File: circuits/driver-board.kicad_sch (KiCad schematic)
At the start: 73 parts, among them J1 Conn_01x18_Female, J2 USB4120-03-C_REVA, J3 Motor_Conn_01x04, J4 Screw_Terminals, J5 Conn_01x06_Female, Q1 SS8050-G, Q2 SS8050-G, SW1 RST_SW_Push, U1 CP2102N-Axx-xQFN24, U2 BA033CC0FP-E2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

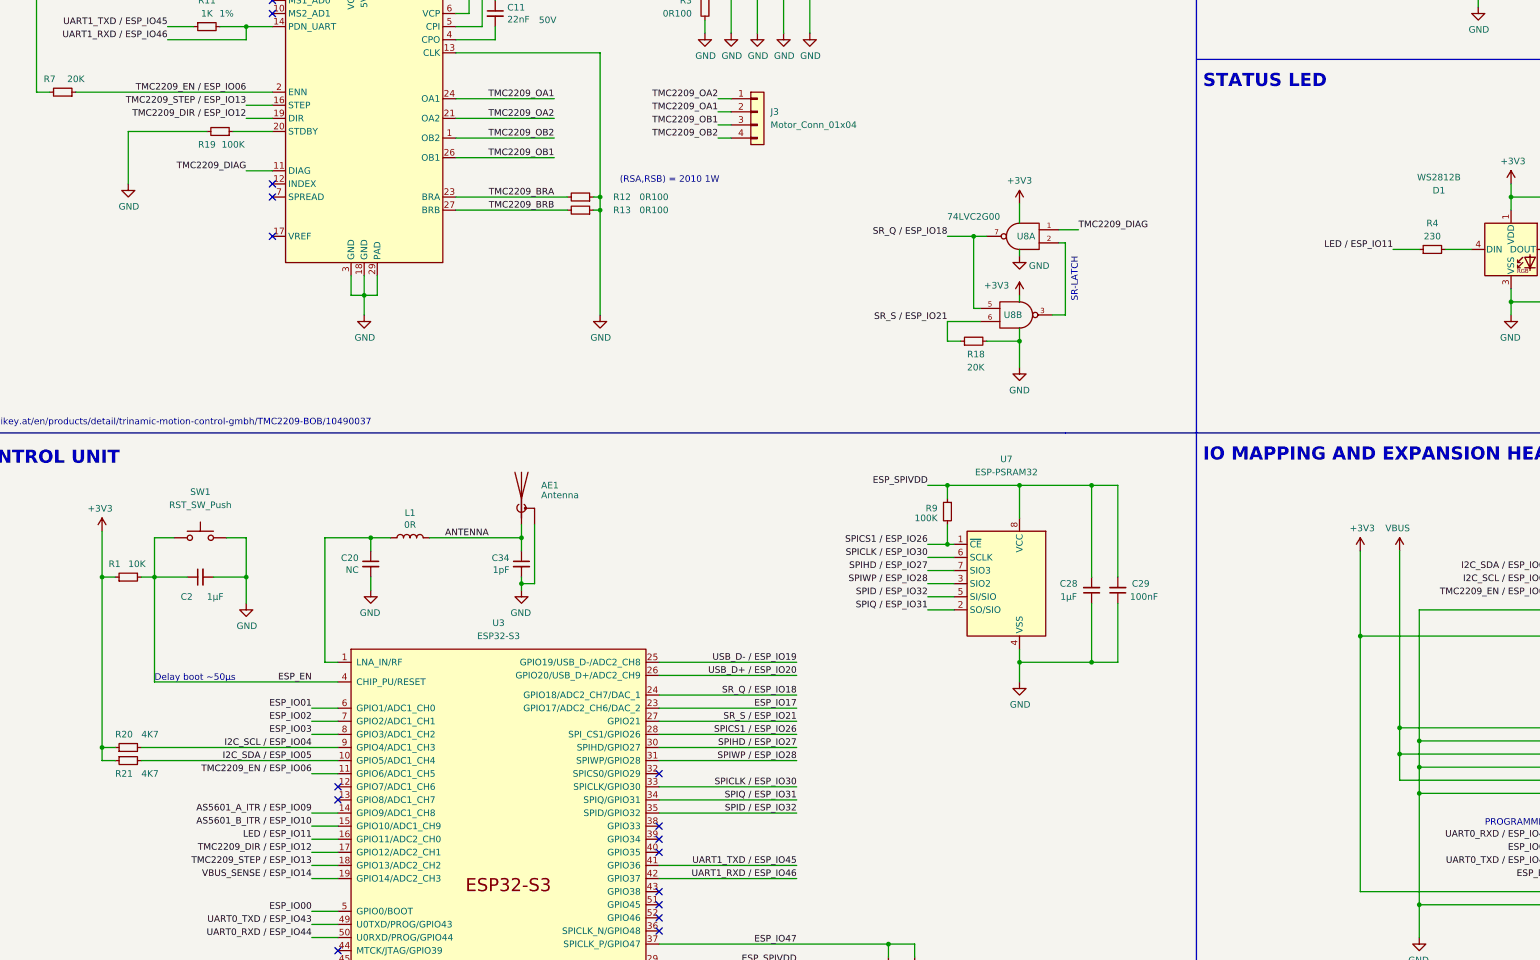
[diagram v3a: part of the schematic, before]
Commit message: replaced a few passive components and improved supply/common loop
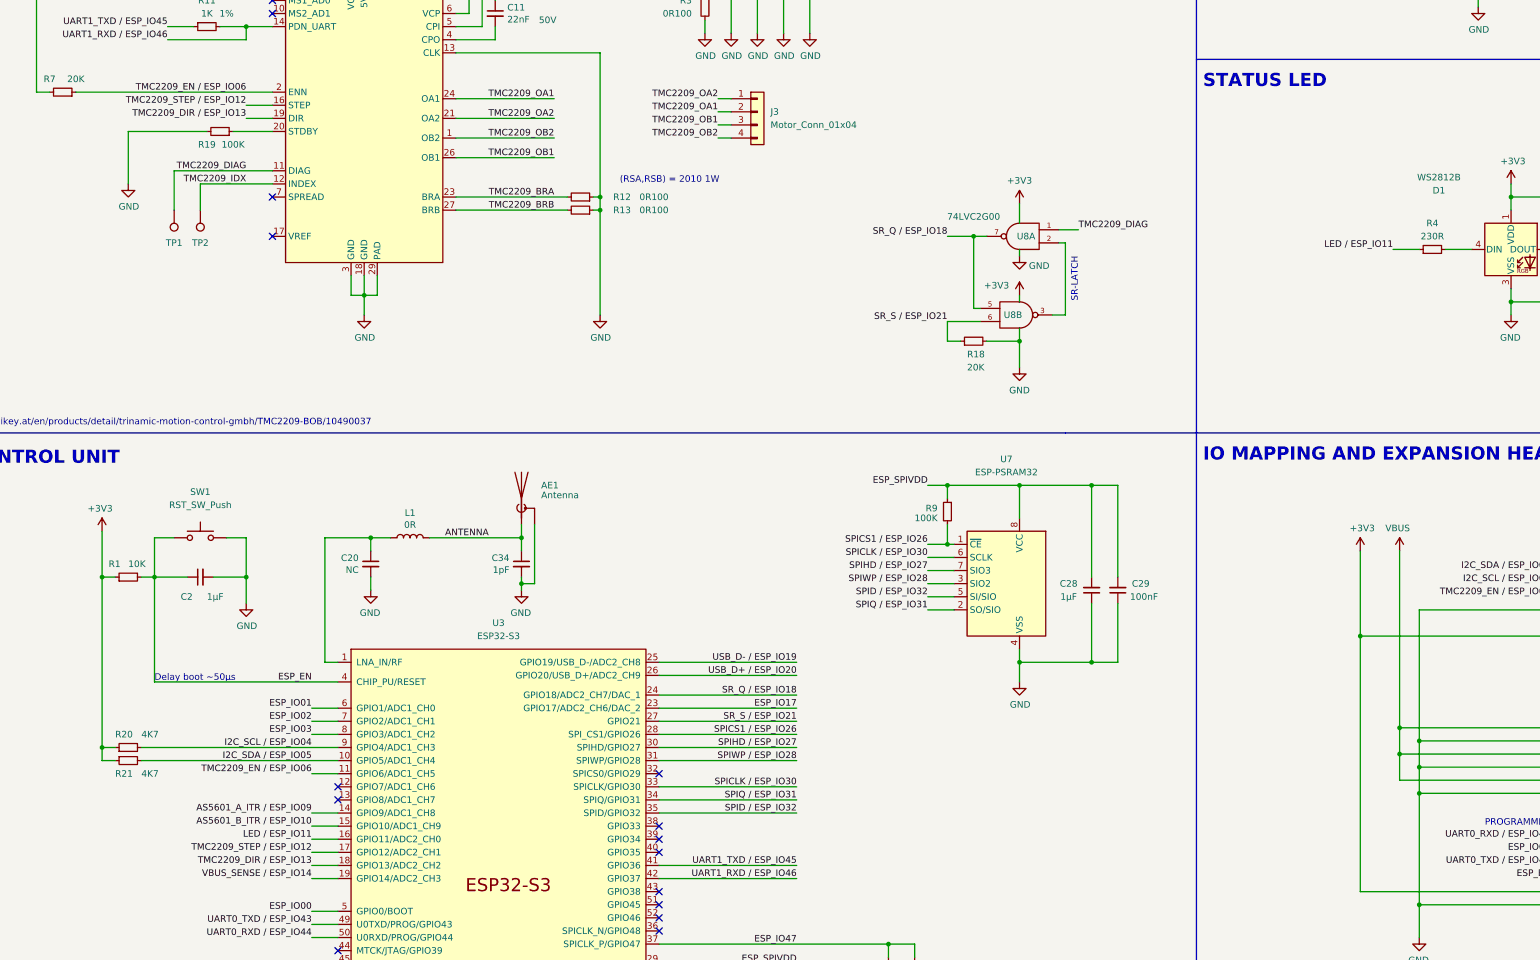
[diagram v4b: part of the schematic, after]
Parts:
- added TP1, TP2: TestPoint, TestPoint:TestPoint_Pad_D1.0mm, symbol Connector:TestPoint
- R4: value 230 -> 230R
- U8: mfr_part_number (none) -> SN74LVC2G00DCT3; mft_part_number SN74LVC2G00DCT3 -> (none)
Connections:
- net TMC2209_DIAG: now also TP1.1
- net TMC2209_IDX: now reaches U5.12 (INDEX)
- net TMC2209_IDX: now also TP2.1
- net TMC2209_DIR / ESP_IO12 renamed TMC2209_DIR / ESP_IO13
- net TMC2209_DIR / ESP_IO13: now also U3.18 (GPIO13/ADC2_CH2); no longer U3.17 (GPIO12/ADC2_CH1)
- net TMC2209_STEP / ESP_IO13 renamed TMC2209_STEP / ESP_IO12
- net TMC2209_STEP / ESP_IO12: now also U3.17 (GPIO12/ADC2_CH1); no longer U3.18 (GPIO13/ADC2_CH2)
- no-connect marks 57 -> 56
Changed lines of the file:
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@@
   (no_connect (at 240.03 260.35))
   (no_connect (at 302.26 248.92))
-  (no_connect (at 227.33 104.14))
   (no_connect (at 85.09 152.4))
   (no_connect (at 473.71 55.88))
@@
     (stroke (width 0) (type default) (color 0 0 0 0))
   )
+  (wire (pts (xy 208.28 101.6) (xy 208.28 109.22))
+    (stroke (width 0) (type default) (color 0 0 0 0))
+  )
   (wire (pts (xy 354.33 173.99) (xy 358.14 173.99))
     (stroke (width 0) (type default) (color 0 0 0 0))
@@
     (stroke (width 0) (type default) (color 0 0 0 0))
   )
-  (wire (pts (xy 302.26 236.22) (xy 328.93 236.22))
+  (wire (pts (xy 302.26 238.76) (xy 328.93 238.76))
     (stroke (width 0) (type default) (color 0 0 0 0))
   )
@@
     (stroke (width 0) (type default) (color 0 0 0 0))
   )
-  (wire (pts (xy 302.26 238.76) (xy 328.93 238.76))
-    (stroke (width 0) (type default) (color 0 0 0 0))
-  )
   (wire (pts (xy 80.01 83.82) (xy 82.55 83.82))
     (stroke (width 0) (type default) (color 0 0 0 0))
@@
     (stroke (width 0) (type default) (color 0 0 0 0))
   )
+  (wire (pts (xy 213.36 104.14) (xy 213.36 109.22))
+    (stroke (width 0) (type default) (color 0 0 0 0))
+  )
   (wire (pts (xy 194.31 171.45) (xy 194.31 180.34))
     (stroke (width 0) (type default) (color 0 0 0 0))
@@
     (stroke (width 0) (type default) (color 0 0 0 0))
   )
+  (wire (pts (xy 302.26 236.22) (xy 328.93 236.22))
+    (stroke (width 0) (type default) (color 0 0 0 0))
+  )
   (wire (pts (xy 327.66 287.02) (xy 327.66 280.67))
     (stroke (width 0) (type default) (color 0 0 0 0))
@@
     (stroke (width 0) (type default) (color 0 0 0 0))
   )
+  (wire (pts (xy 227.33 104.14) (xy 213.36 104.14))
+    (stroke (width 0) (type default) (color 0 0 0 0))
+  )
   (wire (pts (xy 326.39 57.15) (xy 331.47 57.15))
     (stroke (width 0) (type default) (color 0 0 0 0))
@@
     (stroke (width 0) (type default) (color 0 0 0 0))
   )
-  (wire (pts (xy 222.25 101.6) (xy 227.33 101.6))
+  (wire (pts (xy 208.28 101.6) (xy 227.33 101.6))
     (stroke (width 0) (type default) (color 0 0 0 0))
   )
@@
     (effects (font (size 1.27 1.27)) (justify right bottom))
   )
-  (label "TMC2209_STEP {slash} ESP_IO13" (at 234.95 236.22 180)
+  (label "TMC2209_STEP {slash} ESP_IO12" (at 234.95 233.68 180)
     (effects (font (size 1.27 1.27)) (justify right bottom))
   )
@@
     (effects (font (size 1.27 1.27)) (justify right bottom))
   )
-  (label "TMC2209_STEP {slash} ESP_IO13" (at 222.25 88.9 180)
+  (label "TMC2209_STEP {slash} ESP_IO12" (at 222.25 88.9 180)
+    (effects (font (size 1.27 1.27)) (justify right bottom))
+  )
+  (label "TMC2209_IDX" (at 222.25 104.14 180)
     (effects (font (size 1.27 1.27)) (justify right bottom))
   )
@@
     (effects (font (size 1.27 1.27)) (justify right bottom))
   )
-  (label "TMC2209_DIR {slash} ESP_IO12" (at 222.25 91.44 180)
+  (label "TMC2209_DIR {slash} ESP_IO13" (at 222.25 91.44 180)
     (effects (font (size 1.27 1.27)) (justify right bottom))
   )
@@
     (effects (font (size 1.27 1.27)) (justify right bottom))
   )
-  (label "TMC2209_DIR {slash} ESP_IO12" (at 234.95 233.68 180)
+  (label "TMC2209_DIR {slash} ESP_IO13" (at 234.95 236.22 180)
     (effects (font (size 1.27 1.27)) (justify right bottom))
   )
@@
     (in_bom yes) (on_board yes)
     (property "Reference" "R4" (id 0) (at 452.12 111.76 90))
-    (property "Value" "230" (id 1) (at 452.12 114.3 90))
+    (property "Value" "230R" (id 1) (at 452.12 114.3 90))
     (property "Footprint" "Resistor_SMD:R_0402_1005Metric" (id 2) (at 452.12 116.84 0)
       (effects (font (size 1.27 1.27)) hide)
@@
       (effects (font (size 1.27 1.27)) hide)
     )
-    (property "mft_part_number" "SN74LVC2G00DCT3" (id 4) (at 372.11 129.54 0)
+    (property "mfr_part_number" "SN74LVC2G00DCT3" (id 4) (at 372.11 129.54 0)
       (effects (font (size 1.27 1.27)) hide)
     )
@@
       (effects (font (size 1.27 1.27)) hide)
     )
-    (property "mft_part_number" "SN74LVC2G00DCT3" (id 4) (at 372.11 129.54 0)
+    (property "digikey_part_number" "296-SN74LVC2G00DCT3CT-ND" (id 5) (at 372.11 129.54 0)
       (effects (font (size 1.27 1.27)) hide)
     )
-    (property "digikey_part_number" "296-SN74LVC2G00DCT3CT-ND" (id 5) (at 372.11 129.54 0)
+    (property "mfr_part_number" "SN74LVC2G00DCT3" (id 4) (at 372.11 99.06 0)
       (effects (font (size 1.27 1.27)) hide)
     )
@@
     (pin "2")
   )
+  (symbol (lib_id "Connector:TestPoint") (at 208.28 109.22 180) (unit 1)
+    (in_bom yes) (on_board yes)
+    (property "Reference" "TP1" (id 0) (at 208.28 115.57 0))
+    (property "Value" "TestPoint" (id 1) (at 205.74 111.2521 0)
+      (effects (font (size 1.27 1.27)) (justify left) hide)
+    )
+    (property "Footprint" "TestPoint:TestPoint_Pad_D1.0mm" (id 2) (at 203.2 109.22 0)
+      (effects (font (size 1.27 1.27)) hide)
+    )
+    (property "Datasheet" "~" (id 3) (at 203.2 109.22 0)
+      (effects (font (size 1.27 1.27)) hide)
+    )
+    (pin "1")
+  )
   (symbol (lib_id "power:GND") (at 210.82 293.37 0) (unit 1)
     (in_bom yes) (on_board yes)
@@
     (pin "3")
   )
+  (symbol (lib_id "Connector:TestPoint") (at 213.36 109.22 180) (unit 1)
+    (in_bom yes) (on_board yes)
+    (property "Reference" "TP2" (id 0) (at 213.36 115.57 0))
+    (property "Value" "TestPoint" (id 1) (at 210.82 111.2521 0)
+      (effects (font (size 1.27 1.27)) (justify left) hide)
+    )
+    (property "Footprint" "TestPoint:TestPoint_Pad_D1.0mm" (id 2) (at 208.28 109.22 0)
+      (effects (font (size 1.27 1.27)) hide)
+    )
+    (property "Datasheet" "~" (id 3) (at 208.28 109.22 0)
+      (effects (font (size 1.27 1.27)) hide)
+    )
+    (pin "1")
+  )
   (symbol (lib_id "power:GND") (at 321.31 290.83 0) (unit 1)
     (in_bom yes) (on_board yes)
@@
     )
     (path "/00000000-0000-0000-0000-000060d89b88"
-      (reference "R4") (unit 1) (value "230") (footprint "Resistor_SMD:R_0402_1005Metric")
+      (reference "R4") (unit 1) (value "230R") (footprint "Resistor_SMD:R_0402_1005Metric")
     )
     (path "/554372e5-7e5a-402d-8b2d-2a35ad7feffc"
@@
       (reference "SW1") (unit 1) (value "RST_SW_Push") (footprint "Button_Switch_SMD:SW_SPST_B3U-1000P")
     )
+    (path "/927f35e8-55cd-4f24-81b3-f10194e95794"
+      (reference "TP1") (unit 1) (value "TestPoint") (footprint "TestPoint:TestPoint_Pad_D1.0mm")
+    )
+    (path "/c47da70c-bafb-4b99-8294-d393251dcc57"
+      (reference "TP2") (unit 1) (value "TestPoint") (footprint "TestPoint:TestPoint_Pad_D1.0mm")
+    )
     (path "/0e398a34-0a50-47c1-ba62-13809c870cfa"
